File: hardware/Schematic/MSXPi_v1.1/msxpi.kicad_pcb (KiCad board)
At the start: 2 copper layers, 99.9 x 64 mm, 30 parts, among them J1 MSXCART1, J2 JTAG, J3 ROM_SWITCH, J4 Raspberry Pi GPIO, U1 LD117A, U2 EPM3064ALC44, U3 AT28C256

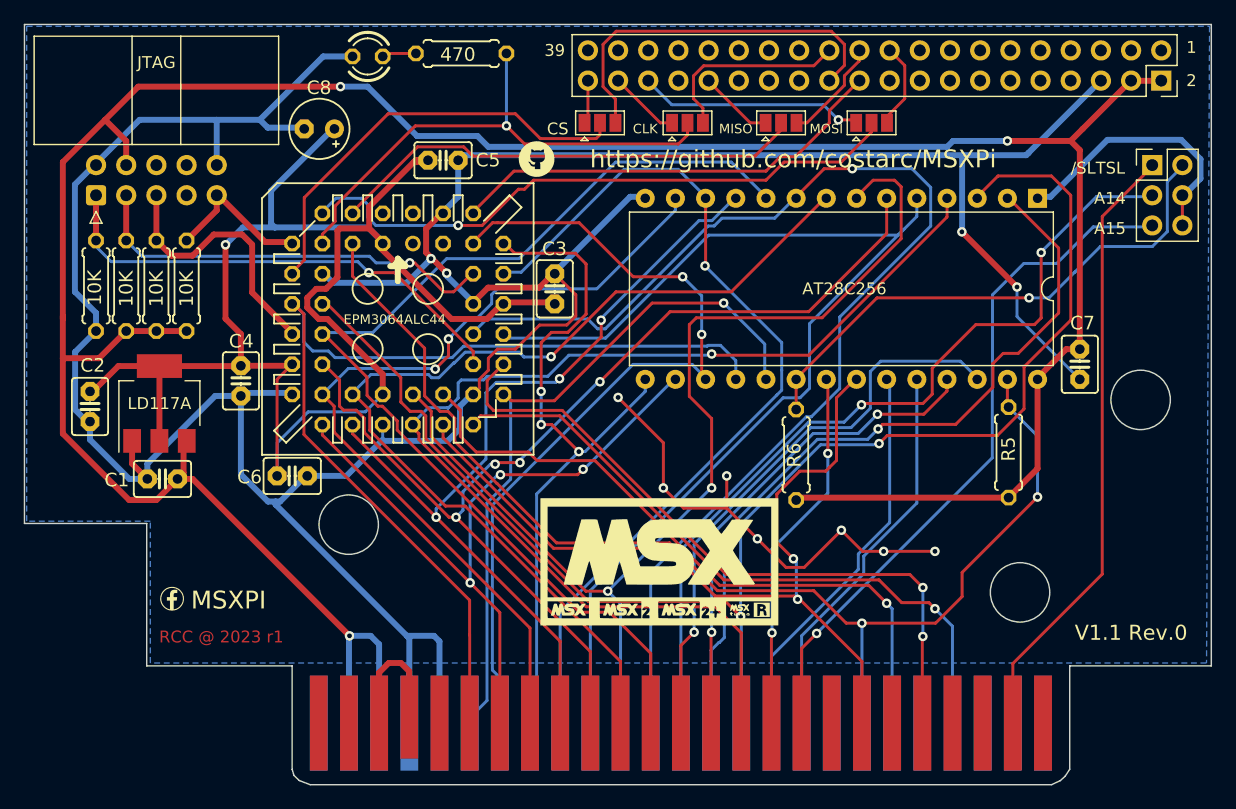
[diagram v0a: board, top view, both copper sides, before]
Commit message: Added game silk to both sides of pcb
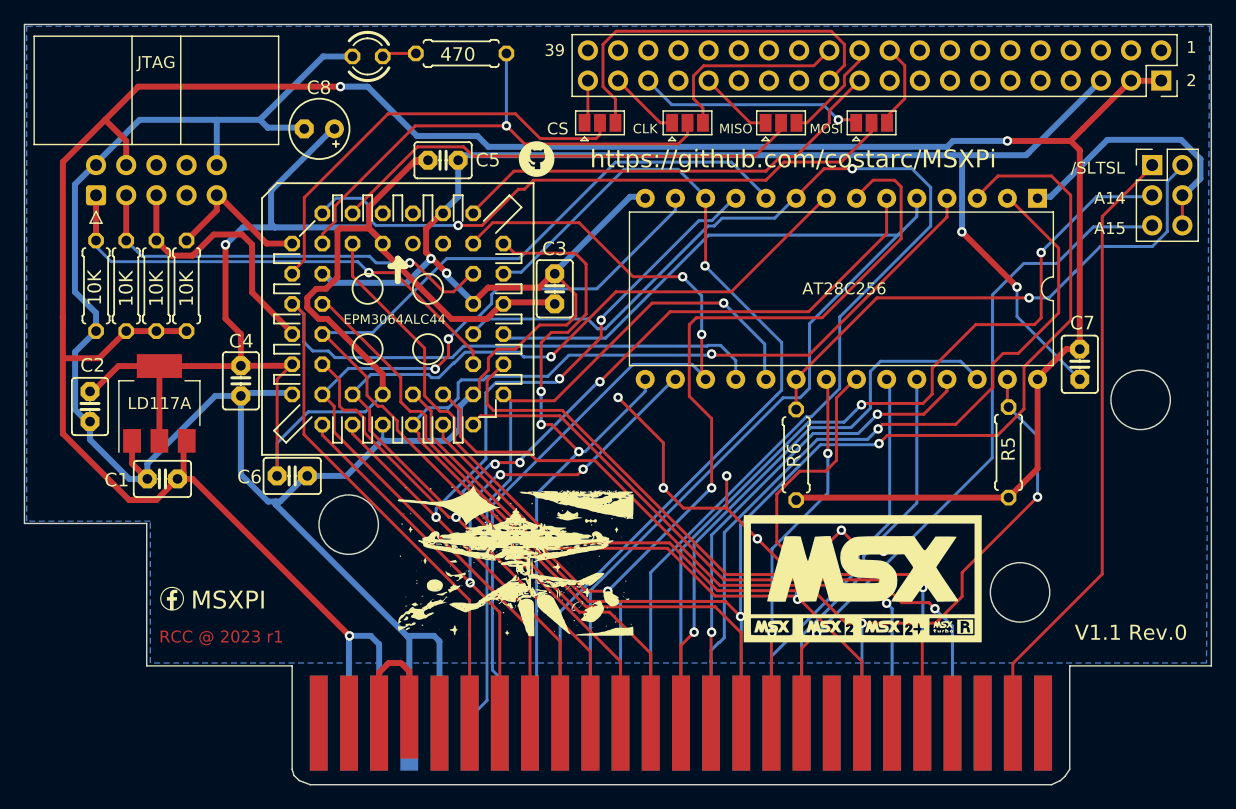
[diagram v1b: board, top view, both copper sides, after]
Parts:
- added G***: LOGO, LOGO, F.Cu at (140.2, 117.9)
- added G***: LOGO, LOGO, B.Cu at (137.7, 92.9)
- added G***: LOGO, LOGO, B.Cu at (111.8, 100.3)
- added G***: LOGO, LOGO, B.Cu at (139.2, 110.0)
- moved G*** 17.2 mm to (169.4, 119.4)
